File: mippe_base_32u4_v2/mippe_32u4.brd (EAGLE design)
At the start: 6.1 x 4.2 mm, 29 parts, among them J2 USB, J5 BURNIN, SW1 BTN-PTS810, U1 ATMEGA32U4-XUMU, Y1 16MHz

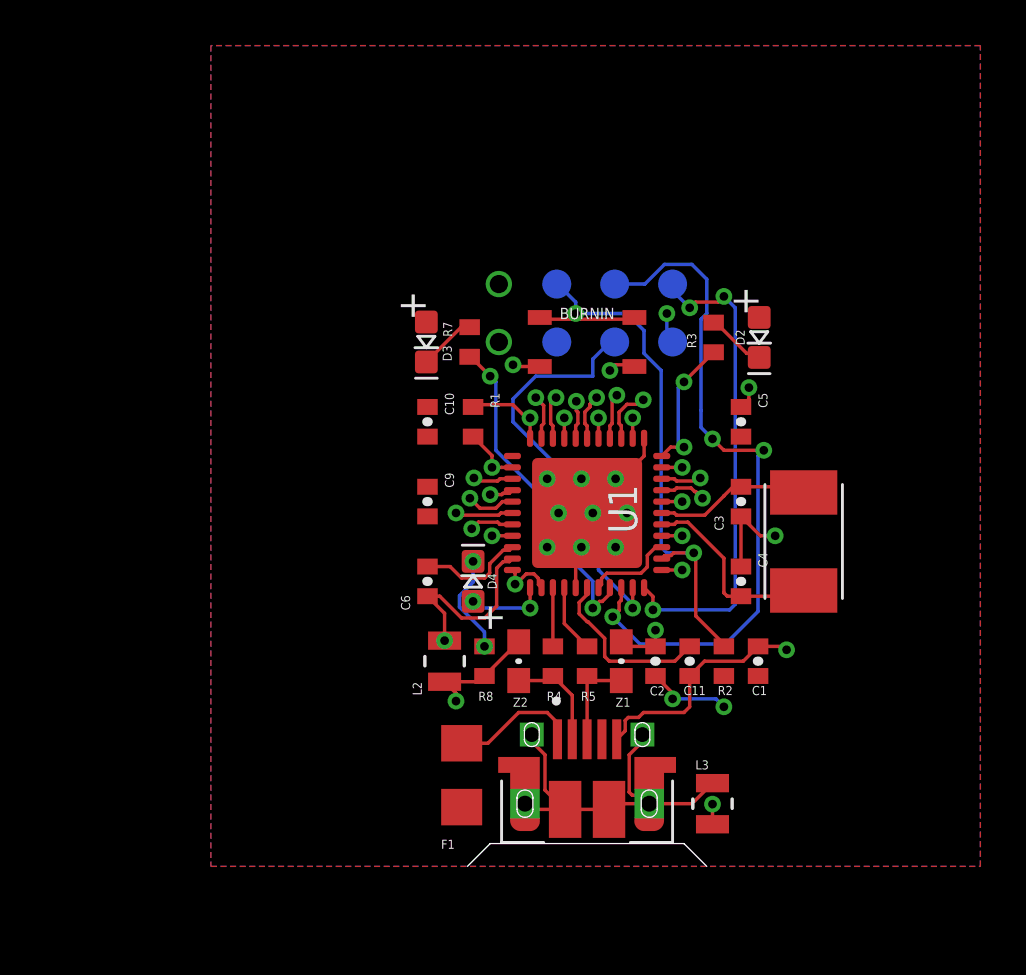
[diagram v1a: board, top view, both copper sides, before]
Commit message: 32u4 0402 rev
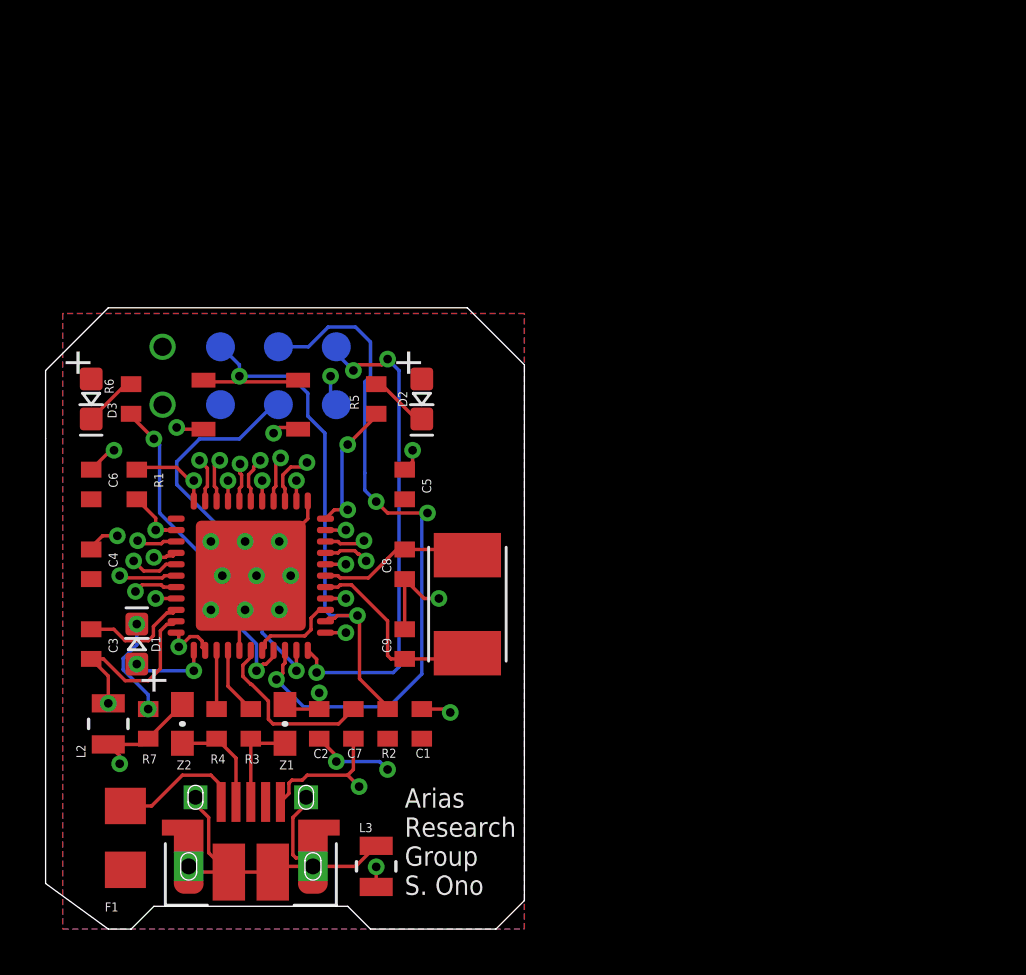
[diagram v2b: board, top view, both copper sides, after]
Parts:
- removed C10, C11: 1uF, scono:0402-CAP
- removed D4: (no value), scono:LED-0603
- removed R8: 330R, scono:R0402
- added C7: 1uF, scono:0402-CAP
- added C8: 18pF, scono:0402-CAP
- added D1: (no value), scono:LED-0603
- added R6: 330R, scono:R0402
- C3, C4: value 18pF -> 0.1uF
- C6: value 0.1uF -> 1uF
- C9: value 0.1uF -> 18pF
- R3: value 330R -> 22R
- R5: value 22R -> 330R
- moved C3 29.2 mm to (-7.00, 9.75)
- moved C4 28.5 mm to (-7.00, 13.2)
- moved R3 26.4 mm to (0.00, 6.25)
- moved R7 21.9 mm to (-4.50, 6.25)
- moved C6 15.4 mm to (-7.00, 16.8), turned to 270 degrees
- moved D2 15.0 mm to (7.50, 20.5)
- moved C1 15.0 mm to (7.50, 6.25)
- moved C2 15.0 mm to (3.00, 6.25)
- moved C5 15.0 mm to (6.75, 16.8)
- moved F1 15.0 mm to (-5.50, 1.25)
- moved J2 15.0 mm to (0.00, 0.00)
- moved J5 15.0 mm to (3.75, 20.2)
- moved L2 15.0 mm to (-6.25, 6.25)
- moved L3 15.0 mm to (5.50, 0.00)
- moved R1 15.0 mm to (-5.00, 16.8)
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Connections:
- net D5* renamed D5
- net D6* renamed D6
- net IO10* renamed IO10
- net IO11* renamed IO11
- net IO13* renamed IO13
- net IO9* renamed IO9
- net 5V: now also C4.2, C6.2; no longer C10.2, C9.2
- net AGND: now also C3.1; no longer C6.1
- net AREF: now also C3.2; no longer C6.2
- net D7: now also D1.A; no longer D4.A
- net D_P: now also R3.1; no longer R5.1
- net GND: now also C6.1, C7.1, C8.1, R7.1; no longer C10.1, C11.1, C3.1, R8.1
- net N$1: now also R5.2; no longer R3.2
- net N$2: now also R6.2; no longer R7.2
- net N$4: now also D1.C, R7.2; no longer D4.C, R8.2
- net RD_P: now also R3.2; no longer R5.2
- net RXLED: now also R6.1; no longer R7.1
- net TXLED: now also R5.1; no longer R3.1
- net UCAP: now also C7.2; no longer C11.2
- net XTAL1: now also C8.2; no longer C3.2
- net XTAL2: now also C9.2; no longer C4.2
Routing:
- net GND: track 38.2 -> 37.6 mm, vias 19 -> 22
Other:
- board size 6.1 x 4.2 mm -> 21 x 27.2 mm
- board text added: "Arias Research Group S. Ono"
- board text removed: "Arias Research Group"
